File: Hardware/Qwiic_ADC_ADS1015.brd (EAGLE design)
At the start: 25.4 x 25.4 mm, 61 parts, among them J4 Screw Pin Terminals, U1 ADS1015

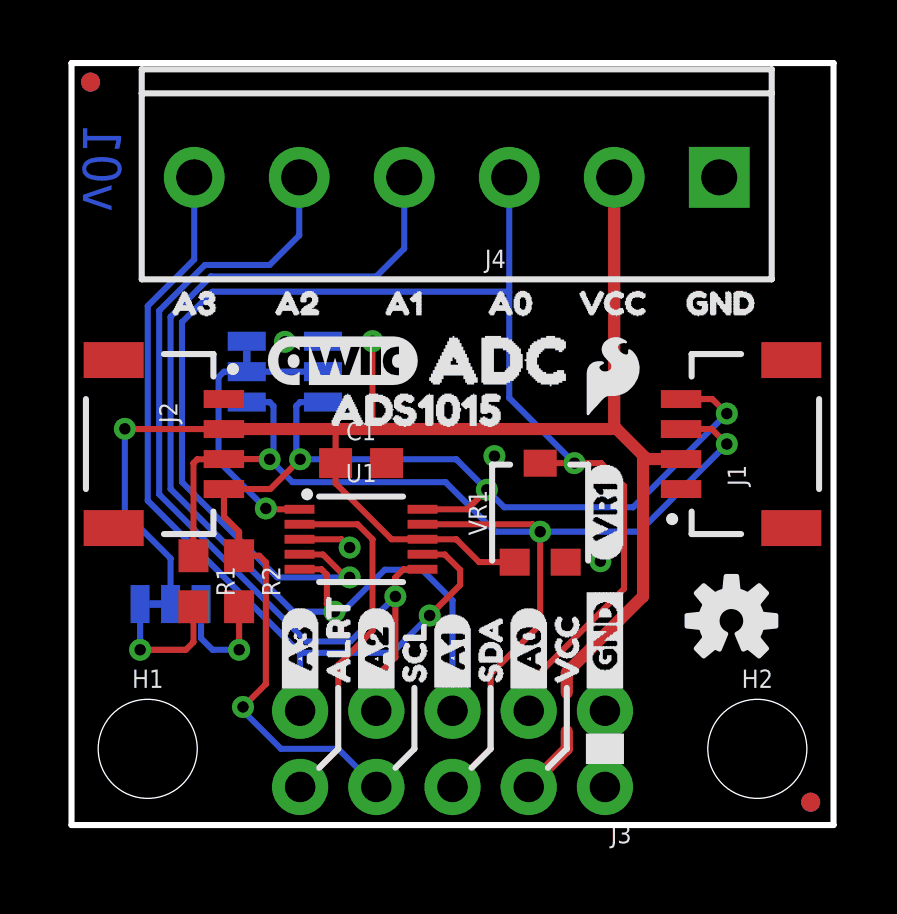
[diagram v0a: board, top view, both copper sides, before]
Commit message: Hardware changes - pre-group review
JP4 label changed to TRIM A0, also labeled trimpot on tops the same.
Product name on bottom silk.
Flipped pin order to have GND on left side of standard I2C pinout.
Bottom labels now show differential inputs names (A0+, A0-, etc.)
Added power LED, moved OSHW logo to bottom silk.
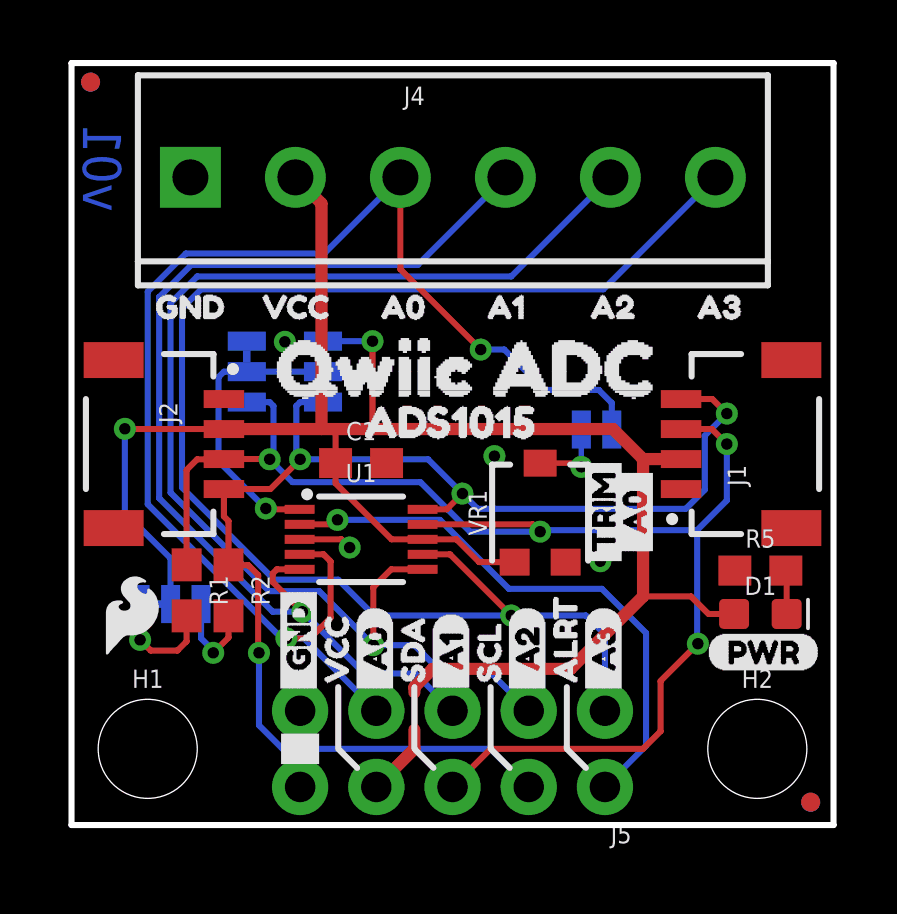
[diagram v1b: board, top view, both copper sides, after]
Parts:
- added D1: RED, SparkFun-LED:LED-0603
- added JP4: (no value), SparkFun-Jumpers:SMT-JUMPER_2_NC_TRACE_NO-SILK
- added R5: 1k, SparkFun-Resistors:0603
- added U$40: (no value), buzzard_labels (18):PWR0
- added U$41: (no value), buzzard_labels (18):I2C1
- added U$42: (no value), buzzard_labels (18):_A0_8
- added U$43: (no value), buzzard_labels (18):QWIIC_ADC2
- U$10: device buzzard_labels (15):_A114 -> buzzard_labels (18):_A0#4
- U$11: device buzzard_labels (16):ADC0 -> buzzard_labels (18):TRIM7
- U$14: device buzzard_labels (15):_A215 -> buzzard_labels (18):_A1#5
- U$15: device Labels:I2C-() -> buzzard_labels (18):_A1#6
- U$16: value QWIIC_LOGO_5MM -> (none); device SparkFun-Aesthetics:QWIIC_5MM -> buzzard_labels (11):QWIIC_ADC0
- U$17: device buzzard_labels (17):VR11 -> buzzard_labels (18):_A0_8
- U$19: device buzzard_labels (15):_A316 -> buzzard_labels (18):TRIM7
- U$9: device buzzard_labels (15):_A013 -> buzzard_labels (18):_A0#3
- moved U$35 22.3 mm to (2.13, 17.3), flipped to the top
- moved U$8 21.2 mm to (22.8, 23.9), flipped to the bottom
- moved LOGO3 17.9 mm to (0.86, 5.36)
- moved J4 17.6 mm to (3.96, 21.6), turned to 0 degrees
- moved U$39 16.1 mm to (20.2, 17.3), flipped to the top
- moved U$34 15.7 mm to (5.69, 17.3), flipped to the top
- moved U$2 15.6 mm to (5.66, 23.9), flipped to the bottom
- moved U$7 14.8 mm to (19.4, 23.9), flipped to the bottom
- moved U$19 14.3 mm to (19.7, 11.9), flipped to the bottom, turned to 0 degrees
- moved U$15 13.3 mm to (17.8, 4.19), turned to 90 degrees
- moved U$20 10.2 mm to (7.57, 4.19), flipped to the bottom
- moved U$29 10.2 mm to (7.57, 4.19), flipped to the top
- moved U$28 10.1 mm to (17.7, 4.19), flipped to the top
- moved U$11 10.1 mm to (17.7, 8.41), turned to 90 degrees
- moved U$38 9.98 mm to (16.6, 17.3), flipped to the top
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- renumbered J3 to J5
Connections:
- new net N$1: JP4.1, VR1.2
- new net N$2: D1.C, R5.2
- net A0: now also J5.7, JP4.2; no longer J5.3, VR1.2
- net A2: now also J5.3; no longer J5.7
- net A3: now also J5.1; no longer J5.9
- net ALRT: now also J5.2; no longer J5.10
- net GND: now also J5.10, J5.9, R5.1; no longer J5.1, J5.2
- net SCL: now also J5.4; no longer J5.8
- net VCC: now also D1.A, J5.8; no longer J5.4
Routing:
- net A3: track 28.8 -> 48.0 mm
- net A2: track 30.0 -> 41.5 mm
- net VCC: track 60.1 -> 68.4 mm
- net ALRT: track 11.9 -> 18.9 mm, vias 0 -> 1
- net SDA: track 41.4 -> 48.1 mm, vias 3 -> 4
- net SCL: track 40.2 -> 44.9 mm
- net A0: track 47.9 -> 45.2 mm
- net N$1: track 0.00 -> 2.67 mm, vias 0 -> 1
- net N$2: track 0.00 -> 1.46 mm
- net N$7: track 4.01 -> 3.24 mm
- net N$8: track 4.59 -> 3.87 mm

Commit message: updated product name silk
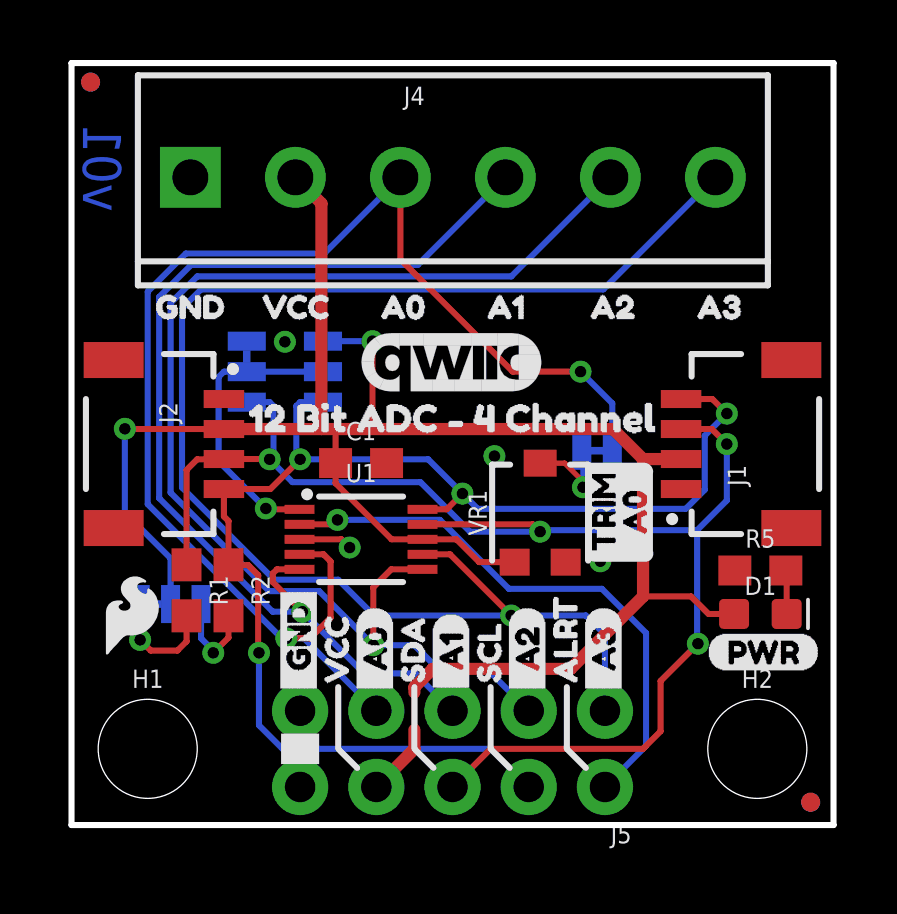
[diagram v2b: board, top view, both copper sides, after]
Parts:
- removed U$22: (no value), buzzard_labels (16):ADS10151
- added U$44: (no value), SparkFun-Aesthetics:QWIIC_6MM
- JP4: device SparkFun-Jumpers:SMT-JUMPER_2_NC_TRACE_NO-SILK -> SparkFun-Jumpers:SMT-JUMPER_2_NC_TRACE_SILK
- U$16: device buzzard_labels (11):QWIIC_ADC0 -> buzzard_labels (20):12_BIT_ADC_#_4_CHANNEL1
- U$43: device buzzard_labels (18):QWIIC_ADC2 -> buzzard_labels (20):12_BIT_ADC_#_4_CHANNEL1
- moved U$43 3.77 mm to (25.6, 15.6)
- moved U$19 2.87 mm to (22.3, 13.0)
- moved U$42 2.87 mm to (22.0, 12.0)
- moved U$16 1.66 mm to (5.11, 13.6)
- moved LOGO1 0.76 mm to (24.1, 16.1)
- moved JP4 0.71 mm to (17.5, 12.5)
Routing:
- net A0: track 45.2 -> 45.7 mm

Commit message: ADDR label on jumper silk on bottom silk
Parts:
- added U$45: (no value), buzzard_labels (22):ADDR0
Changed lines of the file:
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@@
 <layer number="19" name="Unrouted" color="6" fill="1" visible="yes" active="yes"/>
 <layer number="20" name="Dimension" color="15" fill="1" visible="yes" active="yes"/>
-<layer number="21" name="tPlace" color="16" fill="1" visible="yes" active="yes"/>
-<layer number="22" name="bPlace" color="14" fill="1" visible="no" active="yes"/>
-<layer number="23" name="tOrigins" color="15" fill="1" visible="yes" active="yes"/>
+<layer number="21" name="tPlace" color="16" fill="1" visible="no" active="yes"/>
+<layer number="22" name="bPlace" color="14" fill="1" visible="yes" active="yes"/>
+<layer number="23" name="tOrigins" color="15" fill="1" visible="no" active="yes"/>
 <layer number="24" name="bOrigins" color="15" fill="1" visible="yes" active="yes"/>
 <layer number="25" name="tNames" color="7" fill="1" visible="no" active="yes"/>
@@
 <wire x1="16.5608" y1="2.4892" x2="17.145" y2="1.905" width="0.2032" layer="22"/>
 <rectangle x1="6.985" y1="2.032" x2="8.255" y2="3.048" layer="22"/>
-<wire x1="10.8712" y1="18.5674" x2="3.81" y2="18.6182" width="0.2032" layer="22" style="shortdash"/>
+<wire x1="10.8712" y1="18.5674" x2="9.837421875" y2="18.5674" width="0.2032" layer="22" style="shortdash"/>
+<wire x1="4.772659375" y1="18.6182" x2="3.81" y2="18.6182" width="0.2032" layer="22" style="shortdash"/>
 <wire x1="3.81" y1="18.6182" x2="3.81" y2="11.5824" width="0.2032" layer="22" style="shortdash"/>
 <wire x1="3.81" y1="11.5824" x2="10.8712" y2="11.5316" width="0.2032" layer="22" style="shortdash"/>
@@
 <element name="U$16" library="buzzard_labels (20)" package="12_BIT_ADC_#_4_CHANNEL1" value="" x="5.1054" y="13.5636" smashed="yes"/>
 <element name="U$43" library="buzzard_labels (20)" package="12_BIT_ADC_#_4_CHANNEL1" value="" x="25.636221875" y="15.6083" smashed="yes" rot="MR0"/>
+<element name="U$45" library="buzzard_labels (22)" package="ADDR0" value="" x="9.502140625" y="18.6182" smashed="yes" rot="MR0"/>
 </elements>
 <signals>

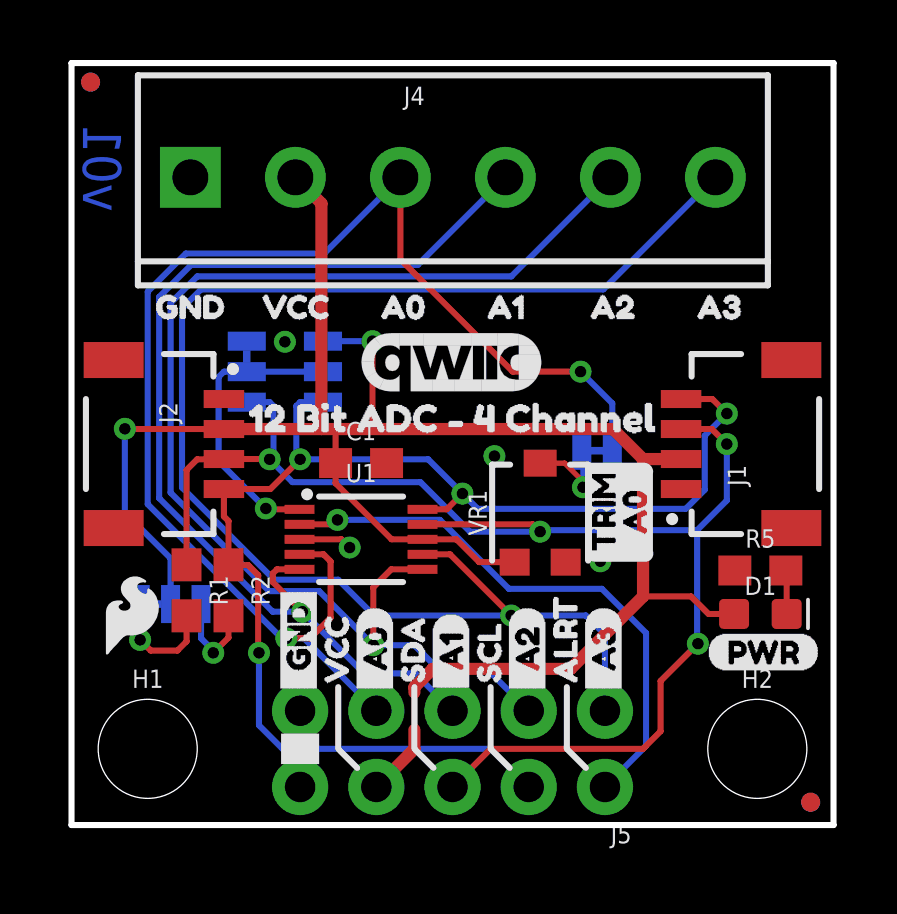
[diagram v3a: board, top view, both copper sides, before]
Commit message: Group design review changes
Moved Trimpot to A3 - so that initial use case can use A0 "as usual".
Improved address jumper labeling
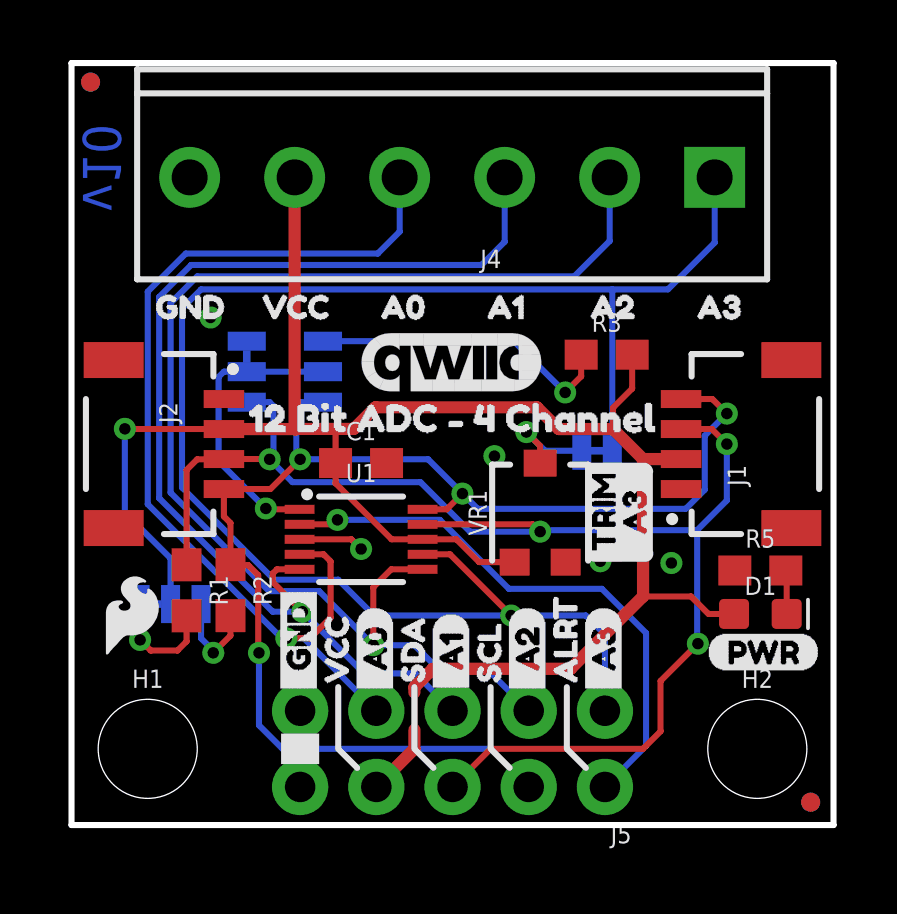
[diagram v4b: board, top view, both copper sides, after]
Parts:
- removed U$13: (no value), buzzard_labels (4):SCL2
- added R3: 4.7k, SparkFun-Resistors:0603
- added U$22: (no value), buzzard_labels (24):_A3_0
- U$12: device buzzard_labels (3):SDA0 -> buzzard_labels (25):0X4B3
- U$17: device buzzard_labels (18):_A0_8 -> buzzard_labels (24):_A3_0
- U$3: device Labels:3V3-TEXT -> buzzard_labels (25):0X4A2
- U$4: device Labels:GND-TEXT-03 -> buzzard_labels (25):0X491
- U$42: device buzzard_labels (18):_A0_8 -> buzzard_labels (26):0X480
- moved J4 17.5 mm to (21.4, 21.6), turned to 180 degrees
- moved U$42 16.6 mm to (5.85, 16.1), turned to 90 degrees
- moved U$3 8.19 mm to (5.90, 10.2), turned to 90 degrees
- moved U$45 5.47 mm to (5.32, 15.1)
- moved U$17 4.62 mm to (22.1, 12.0), flipped to the bottom, turned to 0 degrees
- moved U$12 2.78 mm to (8.41, 10.4), turned to 90 degrees
- moved U$4 1.29 mm to (8.41, 16.0), turned to 90 degrees
- moved R2 0.07 mm to (5.30, 7.83)
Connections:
- new net N$3: JP3.1, R3.1
- net A0: now also J4.4; no longer J4.3, JP4.2
- net A1: now also J4.3; no longer J4.4
- net A2: now also J4.2; no longer J4.5
- net A3: now also J4.1, JP4.2; no longer J4.6
- net GND: now also J4.6; no longer J4.1
- net VCC: now also J4.5, R3.2; no longer J4.2, JP3.1
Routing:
- net A0: track 45.7 -> 33.4 mm, vias 2 -> 1
- net N$3: track 0.00 -> 10.3 mm, vias 0 -> 1
- net A3: track 48.0 -> 54.7 mm
- net VCC: track 68.4 -> 66.8 mm, vias 2 -> 1
- net A1: track 35.2 -> 36.5 mm
- net A2: track 41.5 -> 42.7 mm
- net GND: track 1.78 -> 2.18 mm, vias 4 -> 5
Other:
- board text added: "v10"
- board text removed: "v01"

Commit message: Checklist changes pre double-check
Cleaned up schematic.
Added note for alert ready active high or low.
Adjusted some small stuff for better ground pour flow.
Added SS path on layer 47.
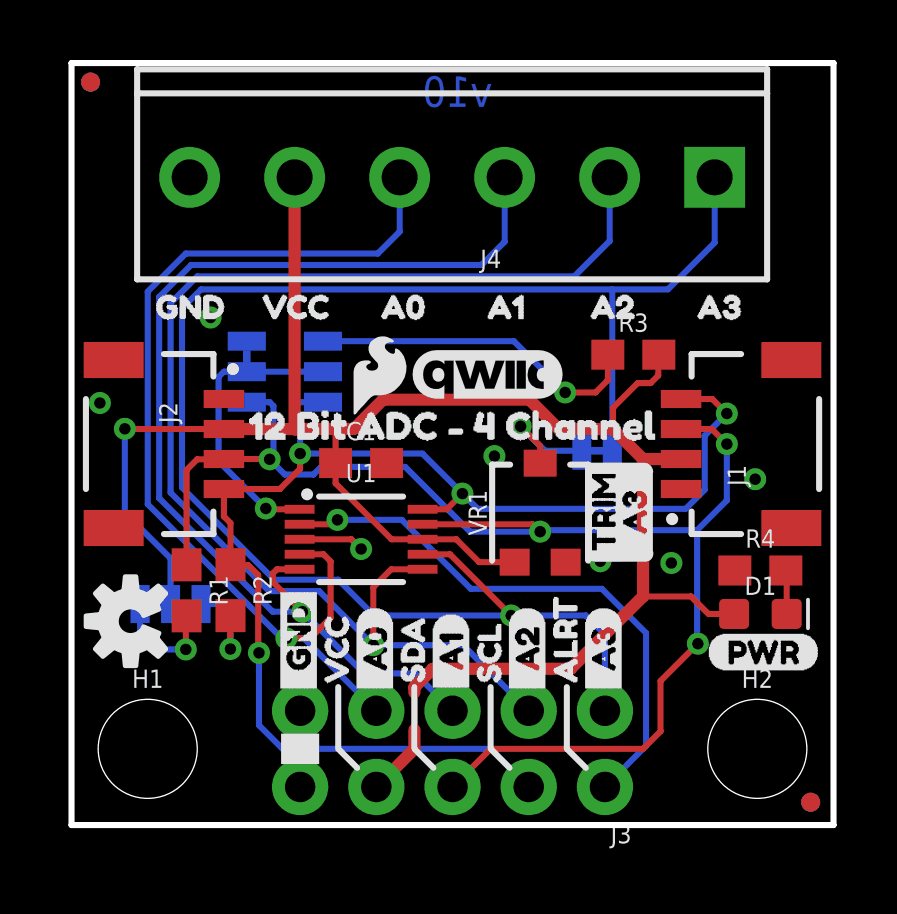
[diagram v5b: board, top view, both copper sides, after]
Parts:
- added U$13: (no value), SparkFun-Aesthetics:OSHW-LOGO-S
- added U$46: (no value), buzzard_labels:ADS10150
- added U$47: (no value), SparkFun-Aesthetics:QWIIC_5MM
- J4: value Screw Pin Terminals -> Screw Pin
- LOGO1: value SFE_LOGO_NAME_FLAME.1_INCH -> SFE_LOGO_NAME.1_INCH; device SparkFun-Aesthetics:SFE_LOGO_NAME_FLAME_.1 -> SparkFun-Aesthetics:SFE_LOGO_NAME_.1
- U$44: device SparkFun-Aesthetics:QWIIC_6MM -> SparkFun-Aesthetics:QWIIC_5MM
- moved LOGO3 13.5 mm to (10.3, 15.0)
- moved LOGO1 6.16 mm to (18.5, 18.7)
- moved U$44 1.20 mm to (13.8, 15.0)
- moved R3 0.89 mm to (18.7, 15.7)
- moved U$16 0.25 mm to (5.11, 13.3)
- renumbered J5 to J3, R5 to R4
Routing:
- net N$3: track 10.3 -> 11.2 mm
- net VCC: track 66.8 -> 67.7 mm
- net N$1: track 3.39 -> 3.92 mm
- net GND: vias 5 -> 7

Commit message: updates post double-check - vias, measures, stubs
1- nudged vias away from being under some silk
2- added measures for distance between standoffs
3- removed wire stubs.
4-moved version in bottom copper to be clear of screw pin terminal bottom silk labels.
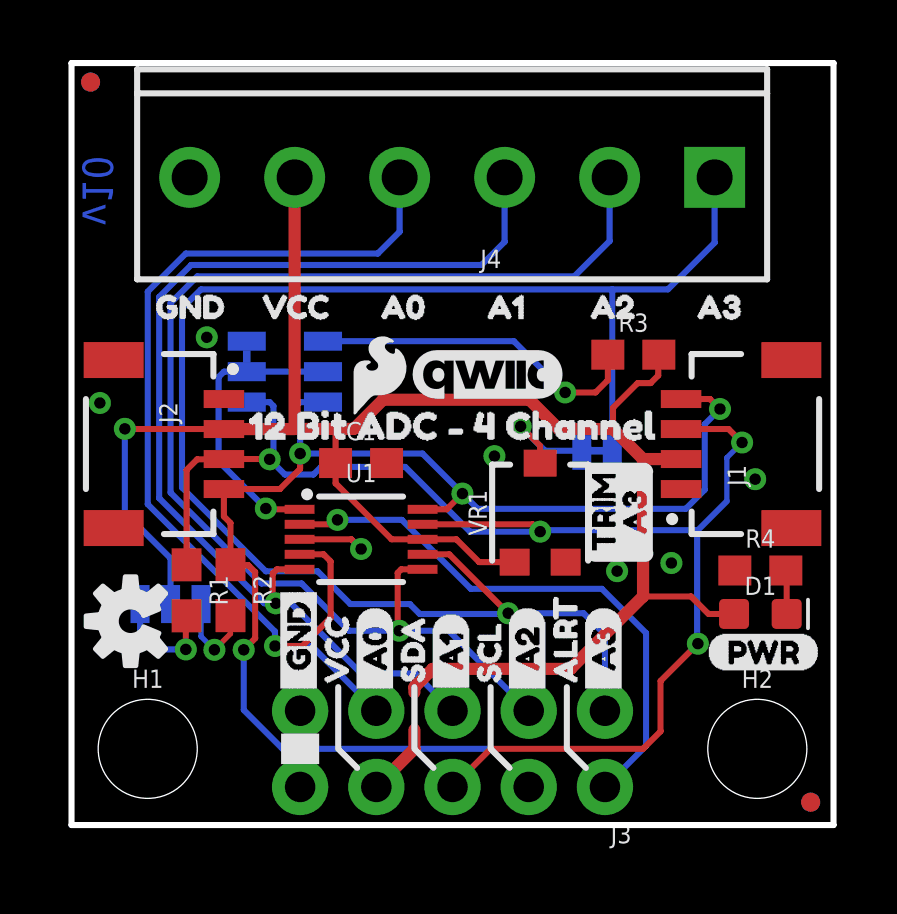
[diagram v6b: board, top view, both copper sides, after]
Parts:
- moved FRAME1 3.81 mm to (-11.4, -14.0)
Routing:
- net A2: track 42.7 -> 41.7 mm
- net SDA: track 48.3 -> 49.1 mm
- net A0: track 33.4 -> 34.1 mm
- net A1: track 36.5 -> 35.8 mm
